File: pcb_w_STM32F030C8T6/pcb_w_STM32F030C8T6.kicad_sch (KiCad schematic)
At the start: 35 parts, among them J1 Conn_01x04, J2 Conn_01x05, J3 USB_B_Mini, SW1 SW_Push, SW2 SW_SPDT, SW3 SW_Push, SW4 SW_Push, SW5 SW_Push, U1 STM32F030C8Tx, U2 IFX27001TFV33

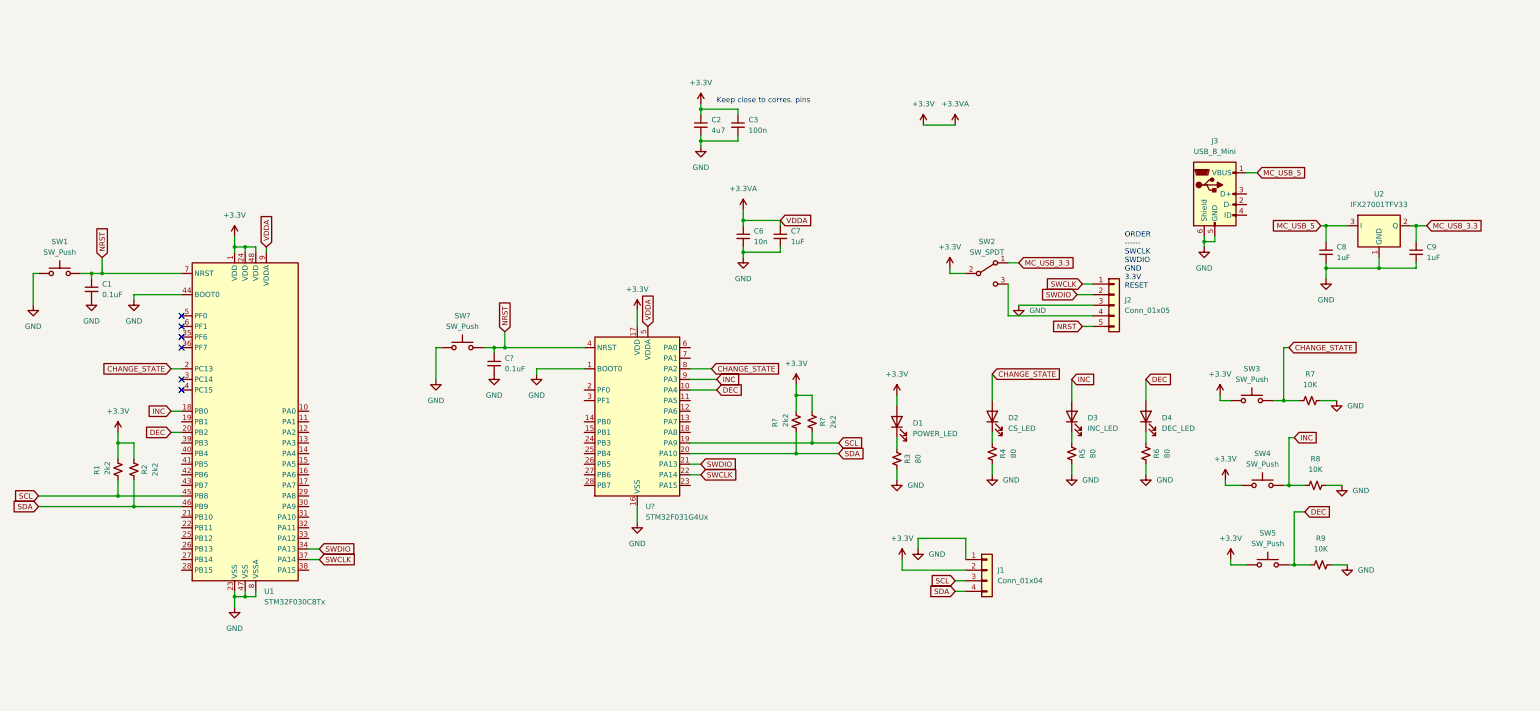
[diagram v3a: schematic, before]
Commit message: changing linear regulator
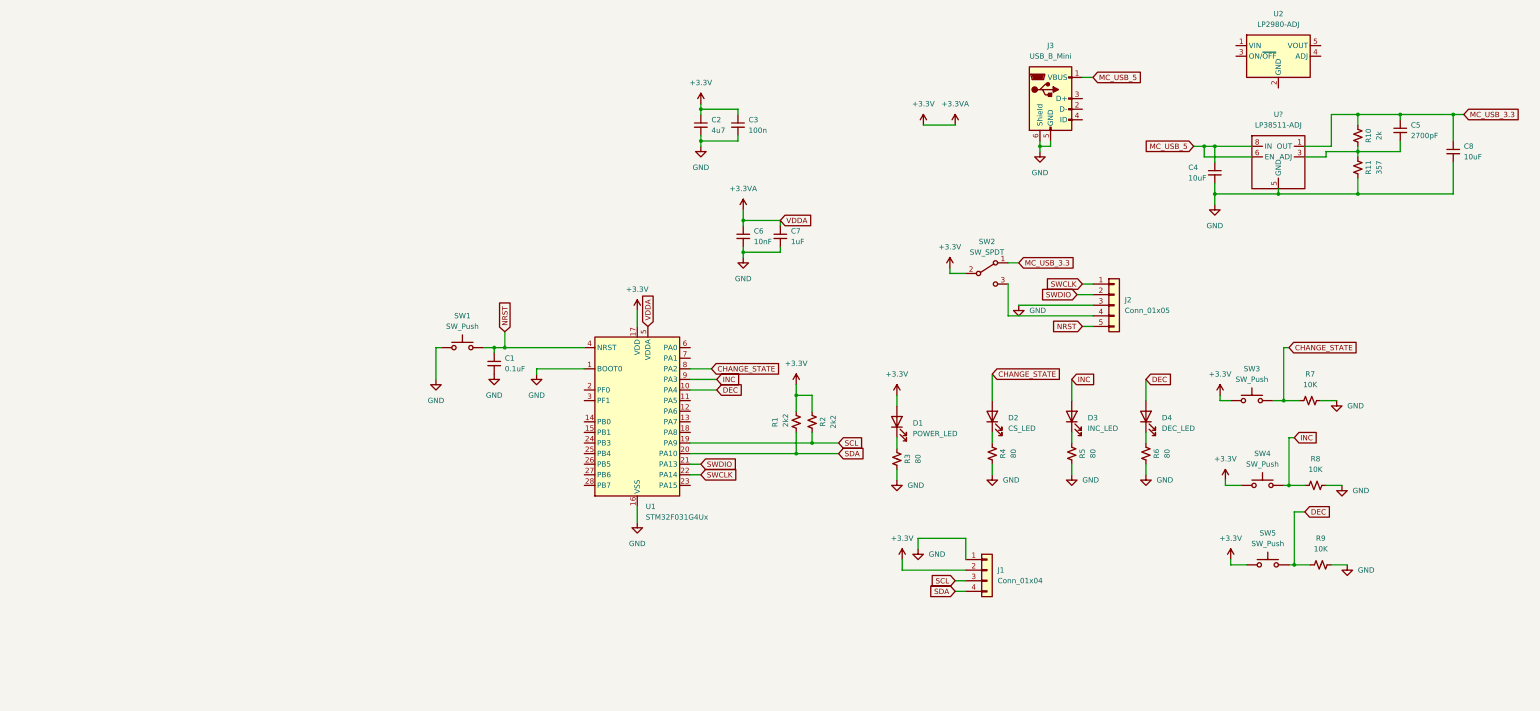
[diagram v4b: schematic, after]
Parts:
- removed C1: 0.1uF, Capacitor_SMD:C_0805_2012Metric_Pad1.18x1.45mm_HandSolder, symbol Device:C_Small
- removed C9: 1uF, Capacitor_SMD:C_0805_2012Metric_Pad1.18x1.45mm_HandSolder, symbol Device:C_Small
- removed R1, R2: 2k2, Resistor_SMD:R_0805_2012Metric_Pad1.20x1.40mm_HandSolder, symbol Device:R_Small_US
- removed SW1: SW_Push, MyLibrary:FSMSMTR-Tactile-Switch-FP, symbol Switch:SW_Push
- removed U1: STM32F030C8Tx, Package_QFP:LQFP-48_7x7mm_P0.5mm, symbol MCU_ST_STM32F0:STM32F030C8Tx
- removed U2: IFX27001TFV33, MyLibrary:SOT23F, symbol Regulator_Linear:IFX27001TFV33
- added C4: 10uF, Capacitor_SMD:C_0805_2012Metric_Pad1.18x1.45mm_HandSolder, symbol Device:C_Small
- added C5: 2700pF, Capacitor_SMD:C_0805_2012Metric_Pad1.18x1.45mm_HandSolder, symbol Device:C_Small
- added R10: 2k, Resistor_SMD:R_0805_2012Metric_Pad1.20x1.40mm_HandSolder, symbol Device:R_Small_US
- added R11: 357, Resistor_SMD:R_0805_2012Metric_Pad1.20x1.40mm_HandSolder, symbol Device:R_Small_US
- added U2: LP2980-ADJ, Package_SO:TI_SO-PowerPAD-8, symbol Regulator_Linear:LP2980-ADJ
- added U?: LP38511-ADJ, symbol New_Library:LP38511-ADJ
- C3: footprint Capacitor_SMD:C_0603_1608Metric_Pad1.08x0.95mm_HandSolder -> Capacitor_SMD:C_0805_2012Metric_Pad1.18x1.45mm_HandSolder; DigiKey Part # GMC10X7R104K50NT -> 0805ZC104KAT2A
- C6: value 10n -> 10nF
- C7: DigiKey Part # GMC21X7R105K16NT -> CL21B105KAFNNNG
- C8: value 1uF -> 10uF; DigiKey Part # GMC21X7R105K16NT -> CL21A106KPFNNNG; JLCPCB Part # C28323 -> (none); LCSC Part Number C28323 -> (none)
- J1: DigiKey Part # SQT-105-01-F-S-RA-001 -> (none)
- R7, R8, R9: DigiKey Part # RN10F1002CT5-50 -> RNCP0805FTD10K0
- gave numbers to parts that had none: 5
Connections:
- net GND: now also C4.2, R11.1, U?.5 (GND)
- net MC_USB_3.3: now also C8.1, C5.1, R10.2, U?.1 (OUT)
- net MC_USB_5: now also C4.1, U?.6 (EN), U?.8 (IN); no longer C8.1
- new net: C5.2, R10.1, R11.2, U?.3 (ADJ)
- no-connect marks 6 -> 0
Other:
- note removed: "Keep close to corres. pins"
- note removed: "ORDER ------ SWCLK SWDIO GND 3.3V RESET"
- moved on the sheet: J3

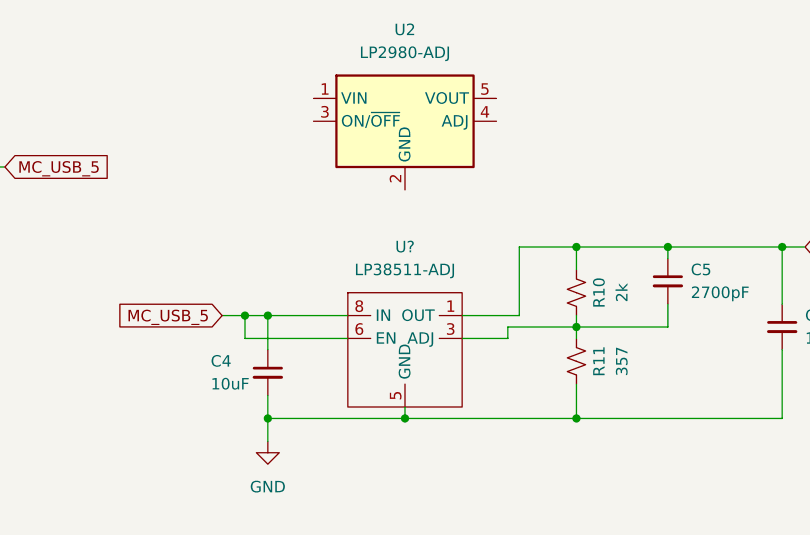
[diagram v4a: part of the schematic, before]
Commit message: finished schematic fixes and finished pcb
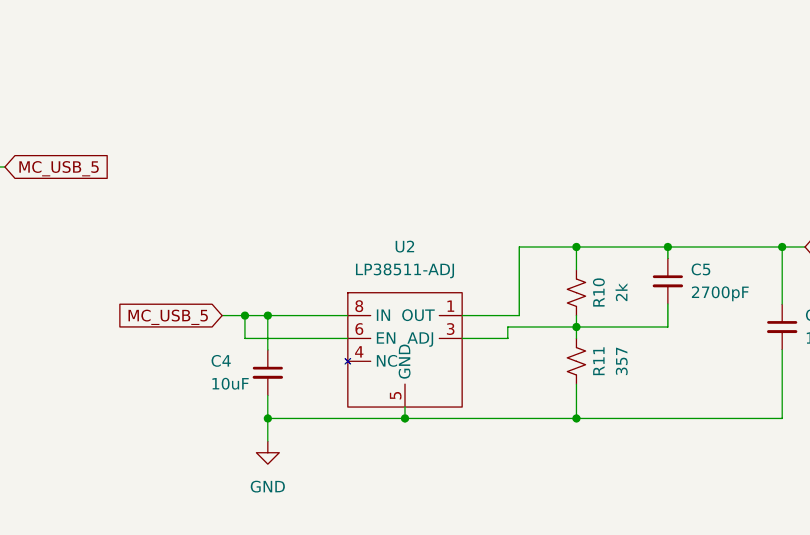
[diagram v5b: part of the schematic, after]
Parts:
- removed U2: LP2980-ADJ, Package_SO:TI_SO-PowerPAD-8, symbol Regulator_Linear:LP2980-ADJ
- removed U?: LP38511-ADJ, symbol New_Library:LP38511-ADJ
- added U2: LP38511-ADJ, MyLibrary:TI_SO-PowerPAD-8-GND_DAP, symbol New_Library:LP38511-ADJ
- C5: DigiKey Part # C2012CH2E272J125AA -> C2012C0G2W272J125AA
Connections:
- net GND: now also U2.5 (GND)
- net MC_USB_3.3: now also U2.1 (OUT)
- net MC_USB_5: now also U2.6 (EN), U2.8 (IN)
- net at C5.2, R10.1, R11.2: now also U2.3 (ADJ)
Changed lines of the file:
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@@
     (pin "2")
-  )
-  (symbol (lib_id "Regulator_Linear:LP2980-ADJ") (at 224.79 20.32 0) (unit 1)
-    (in_bom yes) (on_board yes) (fields_autoplaced)
-    (property "Reference" "U2" (id 0) (at 224.79 10.16 0))
-    (property "Value" "LP2980-ADJ" (id 1) (at 224.79 12.7 0))
-    (property "Footprint" "Package_SO:TI_SO-PowerPAD-8" (id 2) (at 224.79 7.62 0)
-      (effects (font (size 1.27 1.27)) hide)
-    )
-    (property "Datasheet" "http://www.ti.com/lit/ds/symlink/lp2980-adj.pd" (id 3) (at 224.79 12.7 0)
-      (effects (font (size 1.27 1.27)) hide)
-    )
-    (property "DigiKey Part #" "LP38511MR-ADJ/NOPB" (id 4) (at 224.79 20.32 0)
-      (effects (font (size 1.27 1.27)) hide)
-    )
-    (pin "1")
-    (pin "2")
-    (pin "3")
-    (pin "4")
-    (pin "5")
   )
   (symbol (lib_id "power:GND") (at 156.21 120.65 0) (unit 1)
@@
     (pin "1")
   )
-  (symbol (lib_id "New_Library:LP38511-ADJ") (at 224.79 41.91 0) (unit 1)
-    (in_bom yes) (on_board yes) (fields_autoplaced)
-    (property "Reference" "U?" (id 0) (at 224.79 34.29 0))
-    (property "Value" "LP38511-ADJ" (id 1) (at 224.79 36.83 0))
-    (property "Footprint" "" (id 2) (at 226.06 41.91 0)
-      (effects (font (size 1.27 1.27)) hide)
-    )
-    (property "Datasheet" "" (id 3) (at 226.06 41.91 0)
-      (effects (font (size 1.27 1.27)) hide)
-    )
-    (pin "1")
-    (pin "3")
-    (pin "5")
-    (pin "6")
-    (pin "8")
-  )
   (symbol (lib_id "Device:C_Small") (at 254 38.1 0) (unit 1)
     (in_bom yes) (on_board yes)
@@
       (effects (font (size 1.27 1.27)) hide)
     )
-    (property "DigiKey Part #" "C2012CH2E272J125AA" (id 4) (at 254 38.1 0)
+    (property "DigiKey Part #" "C2012C0G2W272J125AA" (id 4) (at 254 38.1 0)
       (effects (font (size 1.27 1.27)) hide)
     )
@@
     (pin "1")
     (pin "2")
+  )
+  (symbol (lib_id "New_Library:LP38511-ADJ") (at 224.79 41.91 0) (unit 1)
+    (in_bom yes) (on_board yes) (fields_autoplaced)
+    (property "Reference" "U2" (id 0) (at 224.79 34.29 0))
+    (property "Value" "LP38511-ADJ" (id 1) (at 224.79 36.83 0))
+    (property "Footprint" "MyLibrary:TI_SO-PowerPAD-8-GND_DAP" (id 2) (at 226.06 41.91 0)
+      (effects (font (size 1.27 1.27)) hide)
+    )
+    (property "Datasheet" "" (id 3) (at 226.06 41.91 0)
+      (effects (font (size 1.27 1.27)) hide)
+    )
+    (property "DigiKey Part #" "LP38511MR-ADJ/NOPB" (id 4) (at 224.79 41.91 0)
+      (effects (font (size 1.27 1.27)) hide)
+    )
+    (pin "1")
+    (pin "3")
+    (pin "4")
+    (pin "5")
+    (pin "6")
+    (pin "8")
   )
   (symbol (lib_id "power:GND") (at 162.56 80.01 0) (unit 1)
@@
       (reference "U1") (unit 1) (value "STM32F031G4Ux") (footprint "Package_DFN_QFN:QFN-28_4x4mm_P0.5mm")
     )
-    (path "/1ae88371-a5ea-46d4-a906-78c34a58a4fc"
-      (reference "U2") (unit 1) (value "LP2980-ADJ") (footprint "Package_SO:TI_SO-PowerPAD-8")
-    )
-    (path "/9210e433-9cda-47e0-a29a-5ccfa16d76f4"
-      (reference "U?") (unit 1) (value "LP38511-ADJ") (footprint "")
-    )
-  )
+    (path "/a870f2c3-9d00-48b6-bb4f-4889d53f13d9"
+      (reference "U2") (unit 1) (value "LP38511-ADJ") (footprint "MyLibrary:TI_SO-PowerPAD-8-GND_DAP")
+    )
+  )
